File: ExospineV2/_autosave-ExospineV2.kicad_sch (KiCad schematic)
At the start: 6 parts, among them J1 GPIO, U1 CAT24C256

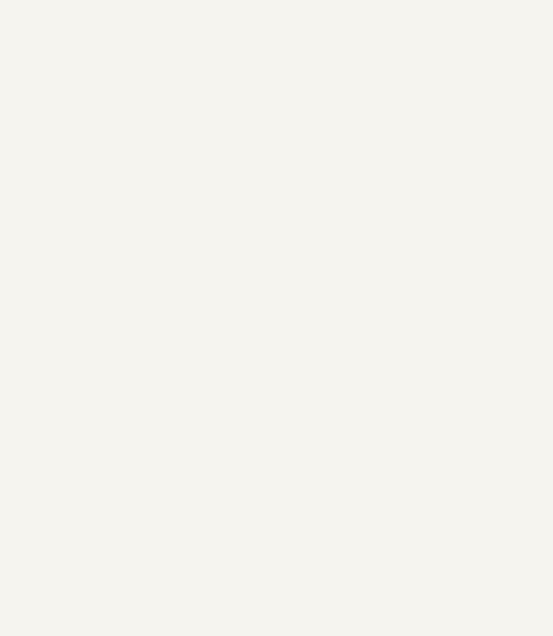
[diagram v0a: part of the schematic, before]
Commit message: changement du schéma, ajout d'une thermistance (contact). Pas besoin d'en mettre plus mais bon exercice
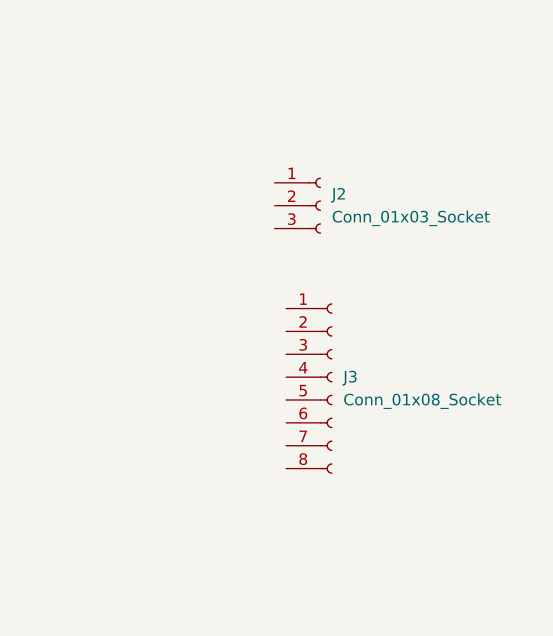
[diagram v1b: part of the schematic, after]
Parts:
- added J2: Conn_01x03_Socket, Connector_JST:JST_EH_B3B-EH-A_1x03_P2.50mm_Vertical, symbol Connector:Conn_01x03_Socket
- added J3: Conn_01x08_Socket, Connector_JST:JST_EH_S8B-EH_1x08_P2.50mm_Horizontal, symbol Connector:Conn_01x08_Socket
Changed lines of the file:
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@@
+    )
+  )
+  (symbol (lib_id "Connector:Conn_01x08_Socket") (at 195.58 71.12 0) (unit 1)
+    (in_bom yes) (on_board yes) (dnp no) (fields_autoplaced)
+    (property "Reference" "J3" (at 196.85 71.12 0)
+      (effects (font (size 1.27 1.27)) (justify left))
+    )
+    (property "Value" "Conn_01x08_Socket" (at 196.85 73.66 0)
+      (effects (font (size 1.27 1.27)) (justify left))
+    )
+    (property "Footprint" "Connector_JST:JST_EH_S8B-EH_1x08_P2.50mm_Horizontal" (at 195.58 71.12 0)
+      (effects (font (size 1.27 1.27)) hide)
+    )
+    (property "Datasheet" "~" (at 195.58 71.12 0)
+      (effects (font (size 1.27 1.27)) hide)
+    )
+    (pin "1")
+    (pin "2")
+    (pin "3")
+    (pin "4")
+    (pin "5")
+    (pin "6")
+    (pin "7")
+    (pin "8")
+    (instances
+      (project "ExospineV2"
+        (path "/e63e39d7-6ac0-4ffd-8aa3-1841a4541b55"
+          (reference "J3") (unit 1)
+        )
+      )
     )
   )
@@
         )
       )
+    )
+  )
+  (symbol (lib_id "Connector:Conn_01x03_Socket") (at 194.31 52.07 0) (unit 1)
+    (in_bom yes) (on_board yes) (dnp no) (fields_autoplaced)
+    (property "Reference" "J2" (at 195.58 50.8 0)
+      (effects (font (size 1.27 1.27)) (justify left))
+    )
+    (property "Value" "Conn_01x03_Socket" (at 195.58 53.34 0)
+      (effects (font (size 1.27 1.27)) (justify left))
+    )
+    (property "Footprint" "Connector_JST:JST_EH_B3B-EH-A_1x03_P2.50mm_Vertical" (at 194.31 52.07 0)
+      (effects (font (size 1.27 1.27)) hide)
+    )
+    (property "Datasheet" "~" (at 194.31 52.07 0)
+      (effects (font (size 1.27 1.27)) hide)
+    )
+    (pin "1")
+    (pin "2")
+    (pin "3")
+    (instances
+      (project "ExospineV2"
+        (path "/e63e39d7-6ac0-4ffd-8aa3-1841a4541b55"
+          (reference "J2") (unit 1)
+        )
+      )
